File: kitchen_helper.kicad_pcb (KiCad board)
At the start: 2 copper layers, 98 x 62.4 mm, 45 parts, among them IC1 ESP32-S3-WROOM-1-N8R8, IC2 FS312F-G, IC3 3v3 Regulator, J1 Bat+, J2 PROG_HDR, J3 DISP_HDR, J4 Temp 1, J5 Temp 2, J6 GND, J7 Battery, Q1 SS8050-G, Q2 SS8050-G, Q3 SS8050-G, Q4 FS8205, Q5 SS8050-G, SW1 SW_Reset, SW2 BTN_LEFT, SW3 BTN_RIGHT, SW4 RotaryEncoder_Switch

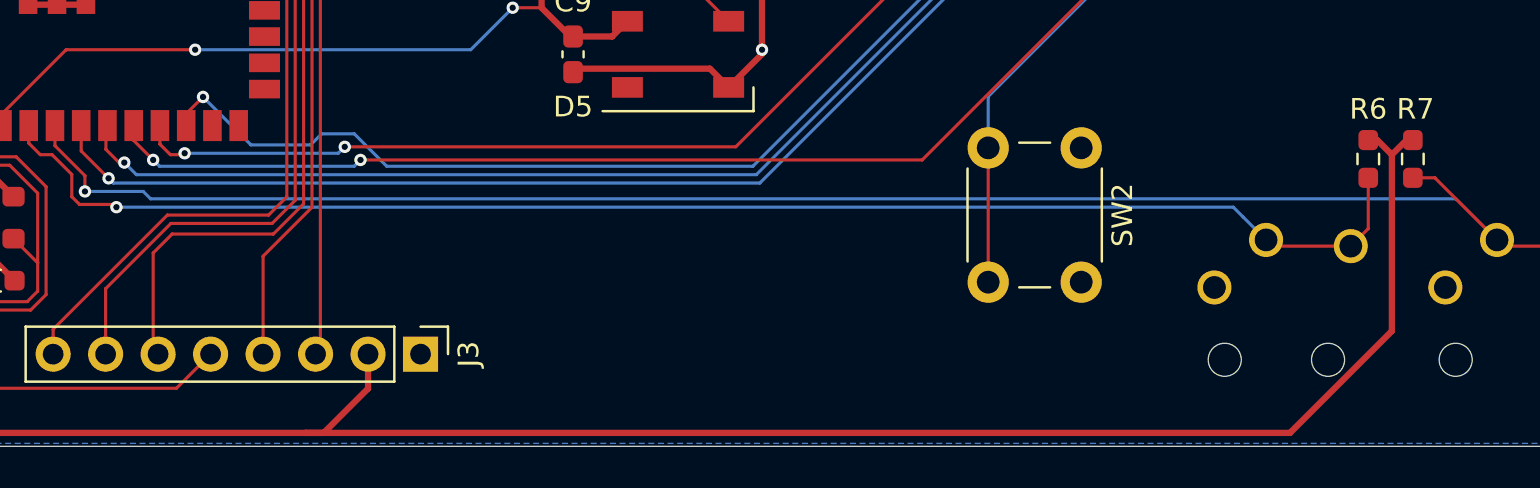
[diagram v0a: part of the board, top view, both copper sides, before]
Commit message: Modifications for ADC ports
- Changed voltage divider resistor to 100k
- Changed the voltage supply for the ADC pins from 3v3 to a GPIO Pin to turn them on only as needeed.
- Deleted some old files
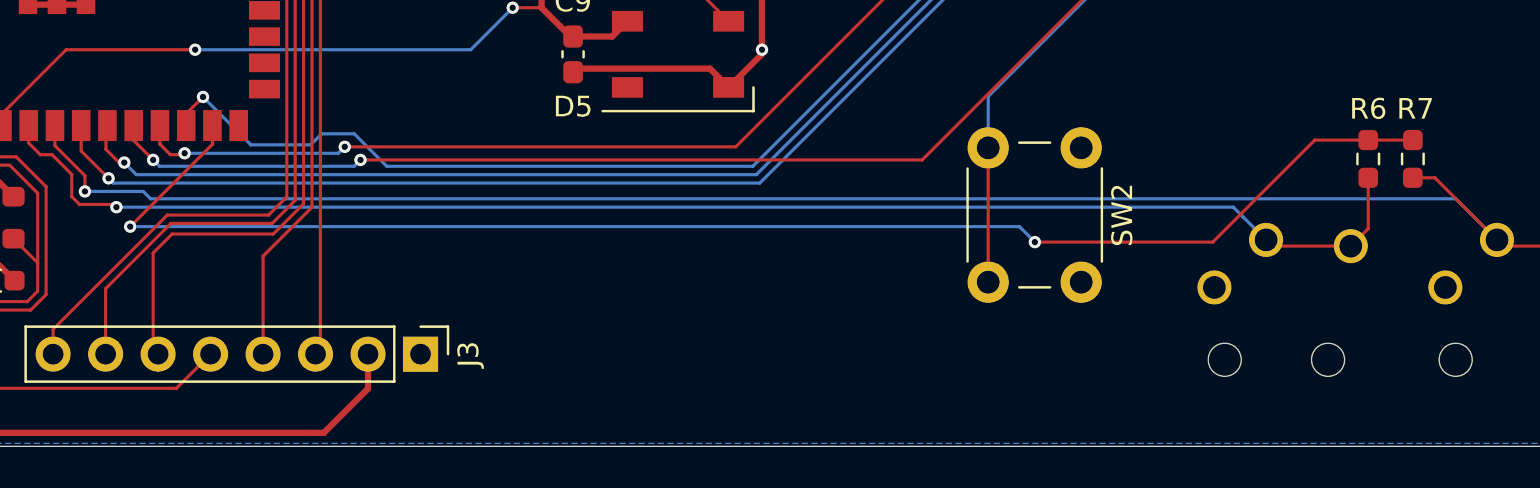
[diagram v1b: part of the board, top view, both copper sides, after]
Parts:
- R6, R7: value 1k -> 100k
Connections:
- IC1 pad 13: unconnected-(IC1-Pad13) -> IO19_ADC_DRV
- R6 pad 1: +3V3 -> IO19_ADC_DRV
- R7 pad 1: +3V3 -> IO19_ADC_DRV
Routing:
- net IO19_ADC_DRV: track 0.00 -> 71.0 mm, vias 0 -> 2
- net +3V3: track 247.3 -> 181.4 mm
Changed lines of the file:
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@@
   (net 16 "REN_BTN_IO18")
   (net 17 "BTNLEFT_IO8")
-  (net 18 "unconnected-(IC1-Pad13)")
+  (net 18 "IO19_ADC_DRV")
   (net 19 "unconnected-(IC1-Pad14)")
   (net 20 "unconnected-(IC1-Pad16)")
@@
   (net 51 "IO36_DISPLAY_SCK")
   (net 52 "BATT+")
-  (net 53 "Net-(Q4-Pad6)")
-  (net 54 "Net-(R9-Pad1)")
-  (net 55 "Net-(Q4-Pad4)")
+  (net 53 "Net-(IC2-Pad1)")
+  (net 54 "Net-(IC2-Pad2)")
+  (net 55 "Net-(IC2-Pad3)")
   (net 56 "unconnected-(IC2-Pad4)")
   (net 57 "Net-(C3-Pad1)")
@@
     (fp_line (start -0.8 0.4125) (end -0.8 -0.4125) (layer "F.Fab") (width 0.1))
     (pad "1" smd roundrect (at -0.9125 0 180) (size 0.975 0.95) (layers "F.Cu" "F.Paste" "F.Mask") (roundrect_rratio 0.25)
-      (net 54 "Net-(R9-Pad1)") (pintype "passive"))
+      (net 54 "Net-(IC2-Pad2)") (pintype "passive"))
     (pad "2" smd roundrect (at 0.9125 0 180) (size 0.975 0.95) (layers "F.Cu" "F.Paste" "F.Mask") (roundrect_rratio 0.25)
       (net 3 "GND") (pintype "passive"))
@@
       (effects (font (size 1 1) (thickness 0.15)))
     )
-    (fp_text value "1k" (at -7.235 -3.035 90) (layer "F.Fab") hide
+    (fp_text value "100k" (at -7.235 -3.035 90) (layer "F.Fab") hide
       (effects (font (size 1 1) (thickness 0.15)))
     )
@@
     (fp_line (start -0.8 0.4125) (end -0.8 -0.4125) (layer "F.Fab") (width 0.1))
     (pad "1" smd roundrect (at -0.9125 0 270) (size 0.975 0.95) (layers "F.Cu" "F.Paste" "F.Mask") (roundrect_rratio 0.25)
-      (net 2 "+3V3") (pintype "passive"))
+      (net 18 "IO19_ADC_DRV") (pintype "passive"))
     (pad "2" smd roundrect (at 0.9125 0 270) (size 0.975 0.95) (layers "F.Cu" "F.Paste" "F.Mask") (roundrect_rratio 0.25)
       (net 12 "TEMP2_AIO7") (pintype "passive"))
@@
       (net 17 "BTNLEFT_IO8") (pinfunction "IO8") (pintype "bidirectional"))
     (pad "13" smd rect (at -8.75 9.98 180) (size 0.9 1.5) (layers "F.Cu" "F.Paste" "F.Mask")
-      (net 18 "unconnected-(IC1-Pad13)") (pinfunction "IO19") (pintype "bidirectional+no_connect"))
+      (net 18 "IO19_ADC_DRV") (pinfunction "IO19") (pintype "bidirectional"))
     (pad "14" smd rect (at -8.75 11.25 180) (size 0.9 1.5) (layers "F.Cu" "F.Paste" "F.Mask")
       (net 19 "unconnected-(IC1-Pad14)") (pinfunction "IO20") (pintype "bidirectional+no_connect"))
@@
       (net 3 "GND") (pinfunction "S2") (pintype "passive"))
     (pad "4" smd rect (at 1.8 -0.95 270) (size 0.6 1.4) (layers "F.Cu" "F.Paste" "F.Mask")
-      (net 55 "Net-(Q4-Pad4)") (pinfunction "G2") (pintype "input"))
+      (net 55 "Net-(IC2-Pad3)") (pinfunction "G2") (pintype "input"))
     (pad "5" smd rect (at 1.8 0 270) (size 0.6 1.4) (layers "F.Cu" "F.Paste" "F.Mask")
       (net 60 "unconnected-(Q4-Pad5)") (pinfunction "D12_2") (pintype "passive+no_connect"))
     (pad "6" smd rect (at 1.8 0.95 270) (size 0.6 1.4) (layers "F.Cu" "F.Paste" "F.Mask")
-      (net 53 "Net-(Q4-Pad6)") (pinfunction "G1") (pintype "input"))
+      (net 53 "Net-(IC2-Pad1)") (pinfunction "G1") (pintype "input"))
     (model ":User models:FS8205.stp"
       (offset (xyz 0.5 0 0.9))
@@
     (fp_line (start -0.8 1.45) (end -0.8 -1.45) (layer "F.Fab") (width 0.1))
     (pad "1" smd rect (at -1.25 -0.95 90) (size 0.6 1.2) (layers "F.Cu" "F.Paste" "F.Mask")
-      (net 53 "Net-(Q4-Pad6)") (pinfunction "OD") (pintype "output"))
+      (net 53 "Net-(IC2-Pad1)") (pinfunction "OD") (pintype "output"))
     (pad "2" smd rect (at -1.25 0 90) (size 0.6 1.2) (layers "F.Cu" "F.Paste" "F.Mask")
-      (net 54 "Net-(R9-Pad1)") (pinfunction "CS") (pintype "passive"))
+      (net 54 "Net-(IC2-Pad2)") (pinfunction "CS") (pintype "passive"))
     (pad "3" smd rect (at -1.25 0.95 90) (size 0.6 1.2) (layers "F.Cu" "F.Paste" "F.Mask")
-      (net 55 "Net-(Q4-Pad4)") (pinfunction "OC") (pintype "output"))
+      (net 55 "Net-(IC2-Pad3)") (pinfunction "OC") (pintype "output"))
     (pad "4" smd rect (at 1.25 0.95 90) (size 0.6 1.2) (layers "F.Cu" "F.Paste" "F.Mask")
       (net 56 "unconnected-(IC2-Pad4)") (pinfunction "TD") (pintype "no_connect"))
@@
       (effects (font (size 1 1) (thickness 0.15)))
     )
-    (fp_text value "1k" (at 0 1.43 90) (layer "F.Fab") hide
+    (fp_text value "100k" (at 0 1.43 90) (layer "F.Fab") hide
       (effects (font (size 1 1) (thickness 0.15)))
     )
@@
     (fp_line (start -0.8 0.4125) (end -0.8 -0.4125) (layer "F.Fab") (width 0.1))
     (pad "1" smd roundrect (at -0.9125 0 270) (size 0.975 0.95) (layers "F.Cu" "F.Paste" "F.Mask") (roundrect_rratio 0.25)
-      (net 2 "+3V3") (pintype "passive"))
+      (net 18 "IO19_ADC_DRV") (pintype "passive"))
     (pad "2" smd roundrect (at 0.9125 0 270) (size 0.975 0.95) (layers "F.Cu" "F.Paste" "F.Mask") (roundrect_rratio 0.25)
       (net 11 "TEMP1_AIO6") (pintype "passive"))
@@
   (segment (start 111.491 107.838) (end 109.347 109.982) (width 0.3048) (layer "F.Cu") (net 2))
   (segment (start 91.32261 97.67108) (end 93.45358 97.67108) (width 0.3048) (layer "F.Cu") (net 2))
-  (segment (start 108.458 109.982) (end 156.110274 109.982) (width 0.3048) (layer "F.Cu") (net 2))
   (segment (start 80.772 101.473) (end 82.423 101.473) (width 0.3048) (layer "F.Cu") (net 2))
   (segment (start 131.13 50.612) (end 130.048 49.53) (width 0.3048) (layer "F.Cu") (net 2))
   (segment (start 79.629 53.34) (end 79.629 100.33) (width 0.3048) (layer "F.Cu") (net 2))
-  (segment (start 161.036 96.52) (end 161.7425 95.8135) (width 0.3048) (layer "F.Cu") (net 2))
   (segment (start 81.407 109.982) (end 108.458 109.982) (width 0.3048) (layer "F.Cu") (net 2))
   (segment (start 84.074 99.822) (end 84.074 98.679) (width 0.3048) (layer "F.Cu") (net 2))
@@
   (segment (start 91.821 101.6) (end 90.734089 100.513089) (width 0.3048) (layer "F.Cu") (net 2))
   (segment (start 80.899 54.61) (end 82.804 54.61) (width 0.3048) (layer "F.Cu") (net 2))
-  (segment (start 161.7425 95.8135) (end 162.052 95.8135) (width 0.3048) (layer "F.Cu") (net 2))
-  (segment (start 156.110274 109.982) (end 161.036 105.056274) (width 0.3048) (layer "F.Cu") (net 2))
-  (segment (start 161.036 96.52) (end 160.3295 95.8135) (width 0.3048) (layer "F.Cu") (net 2))
   (segment (start 89.99 95.811) (end 89.99 95.11) (width 0.3048) (layer "F.Cu") (net 2))
   (segment (start 79.629 108.204) (end 81.407 109.982) (width 0.3048) (layer "F.Cu") (net 2))
-  (segment (start 161.036 105.056274) (end 161.036 96.52) (width 0.3048) (layer "F.Cu") (net 2))
   (segment (start 84.074 98.679) (end 85.852 96.901) (width 0.3048) (layer "F.Cu") (net 2))
   (segment (start 85.852 96.901) (end 88.9 96.901) (width 0.3048) (layer "F.Cu") (net 2))
-  (segment (start 160.3295 95.8135) (end 159.893 95.8135) (width 0.3048) (layer "F.Cu") (net 2))
   (segment (start 111.491 106.172) (end 111.491 107.838) (width 0.3048) (layer "F.Cu") (net 2))
   (segment (start 135.636 56.388) (end 134.62 57.404) (width 0.3048) (layer "F.Cu") (net 3))
@@
   (segment (start 105.82362 96.04462) (end 108.712 96.04462) (width 0.1524) (layer "B.Cu") (net 17))
   (segment (start 130.112644 97.08024) (end 138.996442 88.196442) (width 0.1524) (layer "B.Cu") (net 17))
+  (segment (start 152.37 100.75) (end 157.3065 95.8135) (width 0.1524) (layer "F.Cu") (net 18))
+  (segment (start 143.76 100.75) (end 152.37 100.75) (width 0.1524) (layer "F.Cu") (net 18))
+  (segment (start 159.893 95.8135) (end 162.052 95.8135) (width 0.1524) (layer "F.Cu") (net 18))
+  (segment (start 103.96 95.11) (end 103.96 96.02) (width 0.1524) (layer "F.Cu") (net 18))
+  (segment (start 157.3065 95.8135) (end 159.893 95.8135) (width 0.1524) (layer "F.Cu") (net 18))
+  (segment (start 103.96 96.02) (end 99.98 100) (width 0.1524) (layer "F.Cu") (net 18))
+  (via (at 143.76 100.75) (size 0.6) (drill 0.3) (layers "F.Cu" "B.Cu") (net 18))
+  (via (at 99.98 100) (size 0.6) (drill 0.3) (layers "F.Cu" "B.Cu") (net 18))
+  (segment (start 143.01 100) (end 143.76 100.75) (width 0.1524) (layer "B.Cu") (net 18))
+  (segment (start 99.98 100) (end 143.01 100) (width 0.1524) (layer "B.Cu") (net 18))
   (segment (start 107.559711 88.755289) (end 107.069422 88.265) (width 0.1524) (layer "F.Cu") (net 21))
   (segment (start 96.251 106.172) (end 96.251 104.969919) (width 0.1524) (layer "F.Cu") (net 21))

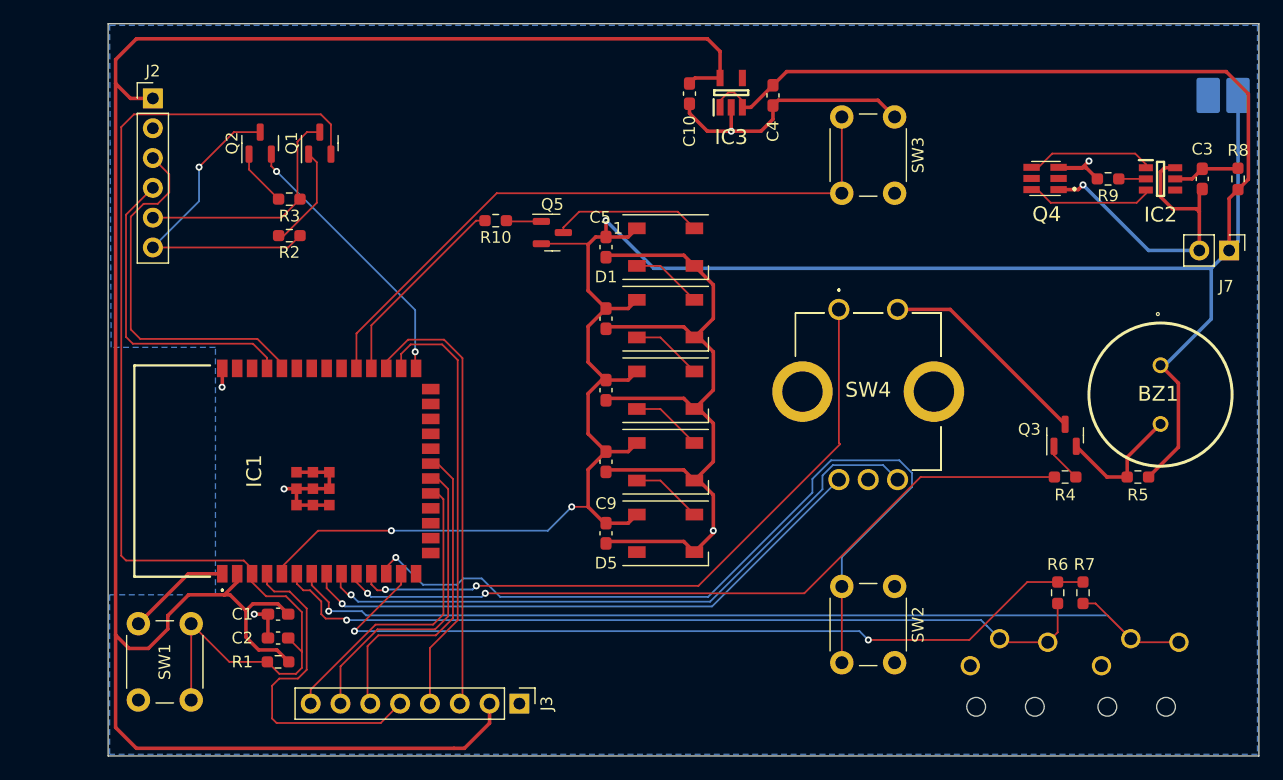
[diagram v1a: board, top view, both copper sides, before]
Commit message: Corrected issues found during schematic verification
- splitted driving lines for both temperature sensors to prevent nfluencing through parallel resistance
- swaped the two directions of the rotary encoder
- Powering the TFT backlight from BATT+ as the voltage drop at the resistor is too much for 3v3
- Added resistor network to directly pull rotary encorder to 3v3
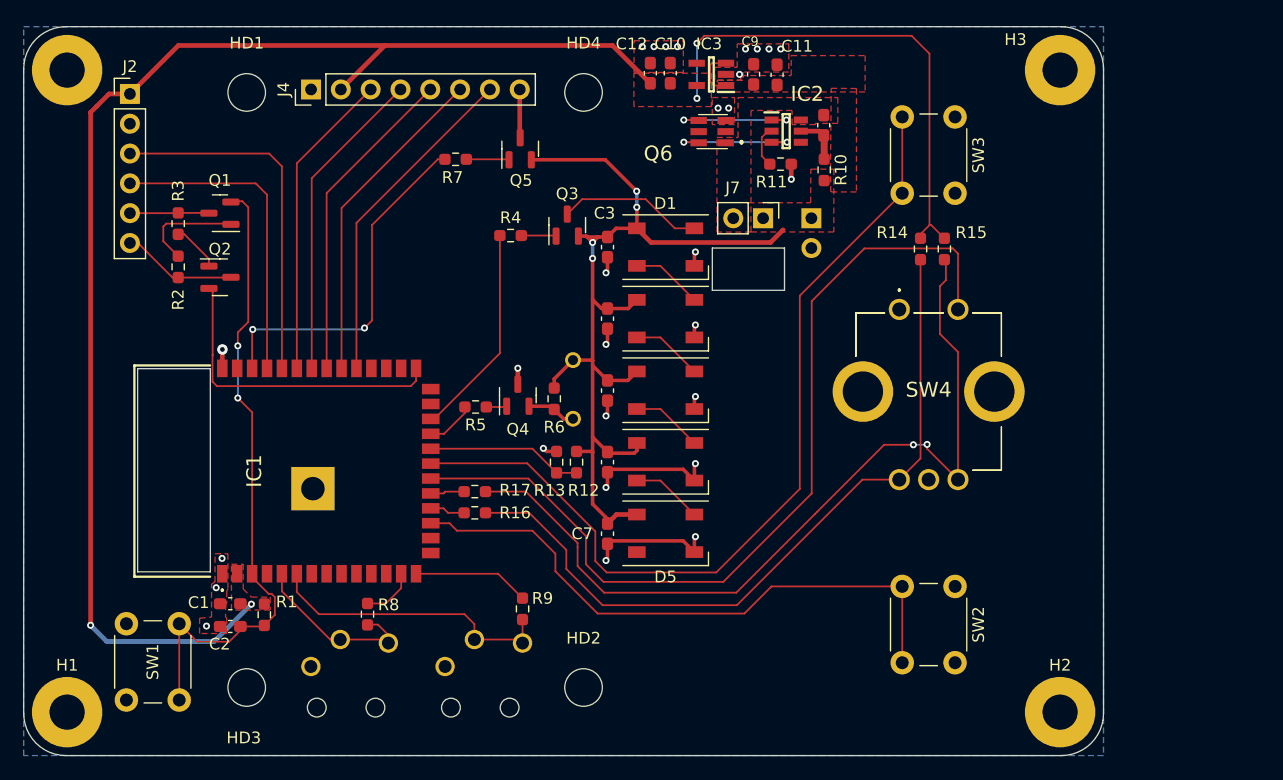
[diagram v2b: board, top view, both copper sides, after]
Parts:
- removed J5: Temp 2, footprints:MJ2509N
- added C11: 1uF, Capacitor_SMD:C_0603_1608Metric_Pad1.08x0.95mm_HandSolder, F.Cu at (136.0, 52.6)
- added C12: 1uF, Capacitor_SMD:C_0603_1608Metric_Pad1.08x0.95mm_HandSolder, F.Cu at (125.2, 52.5)
- added H1: MountingHole, MountingHole:MountingHole_3mm_Pad, F.Cu at (75.5, 106.9)
- added H2: MountingHole, MountingHole:MountingHole_3mm_Pad, F.Cu at (160.1, 106.9)
- added H3: MountingHole, MountingHole:MountingHole_3mm_Pad, F.Cu at (160.1, 52.2)
- added H4: MountingHole, MountingHole:MountingHole_3mm_Pad, F.Cu at (75.5, 52.2)
- added HD1: MountingHole, MountingHole:MountingHole_3.2mm_M3, F.Cu at (90.8, 54.1)
- added HD2: MountingHole, MountingHole:MountingHole_3.2mm_M3, F.Cu at (119.5, 104.8)
- added HD3: MountingHole, MountingHole:MountingHole_3.2mm_M3, F.Cu at (90.8, 104.8)
- added HD4: MountingHole, MountingHole:MountingHole_3.2mm_M3, F.Cu at (119.5, 54.1)
- added Q6: FS8205, footprints:FS8205, F.Cu at (131.1, 57.4)
- added R11: 2k, Resistor_SMD:R_0603_1608Metric_Pad0.98x0.95mm_HandSolder, F.Cu at (136.3, 60.2)
- added R12: 22k, Resistor_SMD:R_0603_1608Metric_Pad0.98x0.95mm_HandSolder, F.Cu at (118.9, 85.6)
- added R13: 22k, Resistor_SMD:R_0603_1608Metric_Pad0.98x0.95mm_HandSolder, F.Cu at (117.2, 85.6)
- added R14: 22k, Resistor_SMD:R_0603_1608Metric_Pad0.98x0.95mm_HandSolder, F.Cu at (148.2, 67.4)
- added R15: 22k, Resistor_SMD:R_0603_1608Metric_Pad0.98x0.95mm_HandSolder, F.Cu at (150.2, 67.4)
- added R16: 1k, Resistor_SMD:R_0603_1608Metric_Pad0.98x0.95mm_HandSolder, F.Cu at (110.2, 89.9)
- added R17: 1k, Resistor_SMD:R_0603_1608Metric_Pad0.98x0.95mm_HandSolder, F.Cu at (110.2, 88.1)
- BZ1: moved to B.Cu
- C3: value 0.1uF -> 100nF
- C4: value 1uF -> 100nF
- C8: value 100nF -> 0.1uF
- C9: value 100nF -> 1uF
- IC3: value 3v3 Regulator -> VReg 3v3
- J1: value Bat+ -> Temp 1; footprint Connector_Wire:SolderWirePad_1x01_SMD+Via_2x3mm -> footprints:MJ2509N
- J3: value DISP_HDR -> Temp 2; footprint Connector_PinHeader_2.54mm:PinHeader_1x08_P2.54mm_Vertical -> footprints:MJ2509N; moved to B.Cu
- J4: value Temp 1 -> DISP_HDR; footprint footprints:MJ2509N -> Connector_PinHeader_2.54mm:PinHeader_1x08_P2.54mm_Vertical; moved to F.Cu
- J6: value GND -> Charger; footprint Connector_Wire:SolderWirePad_1x01_SMD+Via_2x3mm -> Connector_PinHeader_2.54mm:PinHeader_1x02_P2.54mm_Vertical
- Q4: value FS8205 -> SS8050-G; footprint footprints:FS8205 -> Package_TO_SOT_SMD:SOT-23
- R10: value 1k -> 100
- R6, R7: value 100k -> 1k
- R8: value 100 -> 100k
- R9: value 2k -> 100k
- moved J1 89.4 mm to (101.3, 104.6)
- moved R8 82.9 mm to (101.1, 98.6)
- moved J4 79.4 mm to (96.3, 53.8), turned to 90 degrees
- moved R7 65.0 mm to (108.6, 59.8), turned to 180 degrees
- moved R9 61.9 mm to (114.3, 98.1), turned to -90 degrees
- moved R5 56.7 mm to (110.3, 80.9)
- moved R4 51.5 mm to (113.3, 66.3), turned to 180 degrees
- moved C3 51.0 mm to (121.5, 67.3)
- moved BZ1 50.1 mm to (118.6, 79.4), turned to 180 degrees
- moved Q4 49.2 mm to (113.9, 79.9), turned to 90 degrees
- moved Q3 46.0 mm to (118.1, 65.4)
- moved R6 46.0 mm to (117.0, 80.2), turned to 90 degrees
- moved C9 41.1 mm to (134.0, 52.6), turned to 90 degrees
- moved J7 39.8 mm to (134.8, 64.8)
- moved J6 35.4 mm to (138.9, 64.8)
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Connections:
- BZ1 pad 1: BATT+ -> /BATT+
- C3 pad 1: Net-(C3-Pad1) -> /BATT+
- C3 pad 2: BATT- -> GND
- C4 pad 1: BATT+ -> /BATT+
- C5 pad 1: BATT+ -> /BATT+
- C6 pad 1: BATT+ -> /BATT+
- C7 pad 1: BATT+ -> /BATT+
- C8 pad 1: BATT+ -> /Power Management/Bat-In
- C8 pad 2: GND -> /Power Management/BATT-
- C9 pad 1: BATT+ -> /BATT+
- D1 pad 1: BATT+ -> /BATT+
- D2 pad 1: BATT+ -> /BATT+
- D3 pad 1: BATT+ -> /BATT+
- D4 pad 1: BATT+ -> /BATT+
- D5 pad 1: BATT+ -> /BATT+
- IC1 pad 10: IO17_PWM_BUZZ -> unconnected-(IC1-Pad10)
- IC1 pad 11: REN_BTN_IO18 -> unconnected-(IC1-Pad11)
- IC1 pad 12: BTNLEFT_IO8 -> unconnected-(IC1-Pad12)
- IC1 pad 13: IO19_ADC_DRV -> /IO19_ADC_DRV0
- IC1 pad 14: unconnected-(IC1-Pad14) -> /IO19_ADC_DRV1
- IC1 pad 17: unconnected-(IC1-Pad17) -> /BTNLEFT_IO9
- IC1 pad 18: unconnected-(IC1-Pad18) -> /REN_CLK_IO10
- IC1 pad 19: IO11_DISPLAY_BKLT -> /REN_DAT_IO11
- IC1 pad 20: IO12_DISPLAY_CS -> /REN_BTN_IO12
- IC1 pad 21: IO13_DISPLAY_RS -> /BTNRGHT_IO13
- IC1 pad 22: unconnected-(IC1-Pad22) -> /VBat-Check
- IC1 pad 23: unconnected-(IC1-Pad23) -> /IO21_PWM_BUZZ
- IC1 pad 24: unconnected-(IC1-Pad24) -> /IO47_LEDS_DAT
- IC1 pad 28: IO35_DISPLAY_SDA -> unconnected-(IC1-Pad28)
- IC1 pad 29: IO36_DISPLAY_SCK -> unconnected-(IC1-Pad29)
- IC1 pad 30: IO37_LEDS -> unconnected-(IC1-Pad30)
- IC1 pad 31: BTNRGHT_IO38 -> /IO38_DISPLAY_CS
- IC1 pad 32: unconnected-(IC1-Pad32) -> /IO39_DISPLAY_RS
- IC1 pad 33: unconnected-(IC1-Pad33) -> /I40_DISPLAY_RESET
- IC1 pad 34: unconnected-(IC1-Pad34) -> /IO41_DISPLAY_SDA
- IC1 pad 35: unconnected-(IC1-Pad35) -> /IO42_DISPLAY_SCK
- IC1 pad 38: unconnected-(IC1-Pad38) -> /IO02_DISPLAY_BKLT
- IC1 pad 4: IO4_DISPLAY_RESET -> unconnected-(IC1-Pad4)
- IC1 pad 5: BATT+ -> /TEMP1_AIO5
- IC1 pad 6: TEMP1_AIO6 -> /TEMP2_AIO6
- IC1 pad 7: TEMP2_AIO7 -> unconnected-(IC1-Pad7)
- IC1 pad 8: REN_CLK_IO15 -> unconnected-(IC1-Pad8)
- IC1 pad 9: REN_DAT_IO16 -> unconnected-(IC1-Pad9)
- IC2 pad 1: Net-(IC2-Pad1) -> /Power Management/OvrDisChg
- IC2 pad 2: Net-(IC2-Pad2) -> /Power Management/CurrSense
- IC2 pad 3: Net-(IC2-Pad3) -> /Power Management/OvrChg
- IC2 pad 5: Net-(C3-Pad1) -> /Power Management/Bat-In
- IC2 pad 6: BATT- -> /Power Management/BATT-
- IC3 pad 1: BATT+ -> /BATT+
- IC3 pad 3: BATT+ -> /BATT+
- J1 pad 1: BATT+ -> GND
- J3 pad 2: +3V3 -> /TEMP2_AIO6
- J3 pad 3: IO36_DISPLAY_SCK -> /TEMP2_AIO6
- J4 pad 2: TEMP1_AIO6 -> +3V3
- J4 pad 3: TEMP1_AIO6 -> /IO42_DISPLAY_SCK
- J6 pad 1: GND -> /BATT+
- J7 pad 1: BATT+ -> /BATT+
- J7 pad 2: BATT- -> /Power Management/BATT-
- Q3 pad 2: Net-(BZ1-Pad2) -> /BATT+
- Q3 pad 3: GND -> Net-(D1-Pad4)
- Q4 pad 1: BATT- -> Net-(Q4-Pad1)
- Q4 pad 2: unconnected-(Q4-Pad2) -> Net-(BZ1-Pad2)
- Q5 pad 2: BATT+ -> /BATT+
- Q5 pad 3: Net-(D1-Pad4) -> Net-(J4-Pad8)
- R10 pad 1: Net-(Q5-Pad1) -> /Power Management/Bat-In
- R10 pad 2: IO37_LEDS -> /BATT+
- R4 pad 1: IO17_PWM_BUZZ -> Net-(Q3-Pad1)
- R4 pad 2: Net-(Q3-Pad1) -> /IO47_LEDS_DAT
- R5 pad 1: Net-(BZ1-Pad2) -> /IO21_PWM_BUZZ
- R5 pad 2: BATT+ -> Net-(Q4-Pad1)
- R6 pad 1: IO19_ADC_DRV -> Net-(BZ1-Pad2)
- R6 pad 2: TEMP1_AIO6 -> /BATT+
- R7 pad 1: IO19_ADC_DRV -> Net-(Q5-Pad1)
- R7 pad 2: TEMP2_AIO7 -> /IO02_DISPLAY_BKLT
- R8 pad 1: Net-(C3-Pad1) -> /IO19_ADC_DRV0
- R8 pad 2: BATT+ -> /TEMP1_AIO5
- R9 pad 1: Net-(IC2-Pad2) -> /IO19_ADC_DRV1
- R9 pad 2: GND -> /TEMP2_AIO6
- SW2 pad 2: BTNLEFT_IO8 -> /BTNLEFT_IO9
- SW3 pad 2: BTNRGHT_IO38 -> /BTNRGHT_IO13
- SW4 pad 1: REN_BTN_IO18 -> GND
- SW4 pad 2: GND -> /REN_BTN_IO12
- SW4 pad A1: REN_CLK_IO15 -> Net-(R14-Pad1)
- SW4 pad B1: REN_DAT_IO16 -> Net-(R15-Pad1)
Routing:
- net BATT+: track 231.8 -> 0.00 mm, vias 3 -> 0
- net GND: track 143.4 -> 34.3 mm, vias 6 -> 28
- net /BATT+: track 0.00 -> 85.3 mm, vias 0 -> 4
- net TEMP2_AIO7: track 82.6 -> 0.00 mm, vias 1 -> 0
- net /REN_BTN_IO12: track 0.00 -> 76.3 mm
- net /BTNRGHT_IO13: track 0.00 -> 75.0 mm
- net BTNLEFT_IO8: track 72.1 -> 0.00 mm, vias 1 -> 0
- net Net-(R15-Pad1): track 0.00 -> 71.3 mm, vias 0 -> 2
- net TEMP1_AIO6: track 71.2 -> 0.00 mm, vias 1 -> 0
- net IO19_ADC_DRV: track 71.0 -> 0.00 mm, vias 2 -> 0
- net IO17_PWM_BUZZ: track 64.9 -> 0.00 mm, vias 2 -> 0
- net Net-(R14-Pad1): track 0.00 -> 63.4 mm
- net REN_BTN_IO18: track 57.7 -> 0.00 mm, vias 2 -> 0
- net BTNRGHT_IO38: track 55.8 -> 0.00 mm
- net REN_DAT_IO16: track 55.2 -> 0.00 mm, vias 1 -> 0
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- added copper zone on F.Cu, net +3V3
- added copper zone on F.Cu, net /BATT+
- added copper zone on F.Cu, net /Power Management/BATT-
- added copper zone on F.Cu, net GND
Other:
- board size 98 x 62.4 mm -> 92 x 62.1 mm
